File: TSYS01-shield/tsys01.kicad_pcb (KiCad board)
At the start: 2 copper layers, 20 x 24 mm, 25 parts, among them P1 CONN_01X02, P2 CONN_01X04, U1 TSYS01, U2 SP6213

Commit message: First production version
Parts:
- added G***: LOGO, LOGO, F.Cu at (43.1, 57.2)
- added G***: LOGO, LOGO, F.Cu at (43.7, 66.9)
- P1: footprint Pin_Headers:Pin_Header_Angled_1x02 -> pin_header_fork:Pin_Header_Angled_SMD_1x02
- P2: footprint Pin_Headers:Pin_Header_Angled_1x04 -> pin_header_fork:Pin_Header_Angled_SMD_1x04
- moved JP3 9.00 mm to (29.0, 52.1), turned to 270 degrees
- moved JP4 7.97 mm to (29.0, 53.6), turned to 270 degrees
- moved U1 6.94 mm to (34.3, 51.6)
- moved C3 4.50 mm to (30.6, 52.8), turned to 270 degrees
- moved C2 4.04 mm to (31.7, 59.7), turned to 270 degrees
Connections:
- U1 pad 17: (no net) -> /PAD
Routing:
- net +3V3: track 27.7 -> 42.9 mm, vias 4 -> 5
- net GNDA: track 16.4 -> 27.1 mm, vias 8 -> 5
- net Net-(D2-Pad2): track 8.02 -> 16.5 mm
- net Net-(D4-Pad2): track 5.58 -> 13.2 mm
- net Net-(D6-Pad2): track 6.07 -> 13.3 mm
- net /PAD: track 0.00 -> 5.97 mm, vias 0 -> 4
- net /EN: track 9.90 -> 15.4 mm
- net /Vin: track 12.3 -> 11.8 mm, vias 0 -> 2
- added copper zone on B.Cu, net /PAD
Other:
- board size 20 x 24 mm -> 28 x 28 mm
- net class Default: clearance 0.2 -> 0.19
- rule trace_clearance: 0.2 -> 0.19
- board text added: "5V"
- board text added: "CS"
- board text added: "GND"
- board text added: "I2C mode: R2 NO-POP, I2C Address: D8 Pull down OR D9 Pull up"
- board text added: "JMP1: always ON JMP2: ON when CS HIGH !JMP1 & !JMP2: undefined JMP1 & JMP2: short circuit"
- board text added: "JMP3: I2C mode JMP4: SPI mode !JMP3 & !JMP4: undefined JMP3 & JMP4: short circuit"
- board text added: "MISO"
- board text added: "MOSI/SDA"
- board text added: "Open Hardware"
- board text added: "SCLK/SCL"
- board text added: "SPI MODE: JMP1 only"
- board text added: "TSYS01 High precision temperature sensor board"
- board text added: "https://github.com/ ojousima/kon-41.3131"

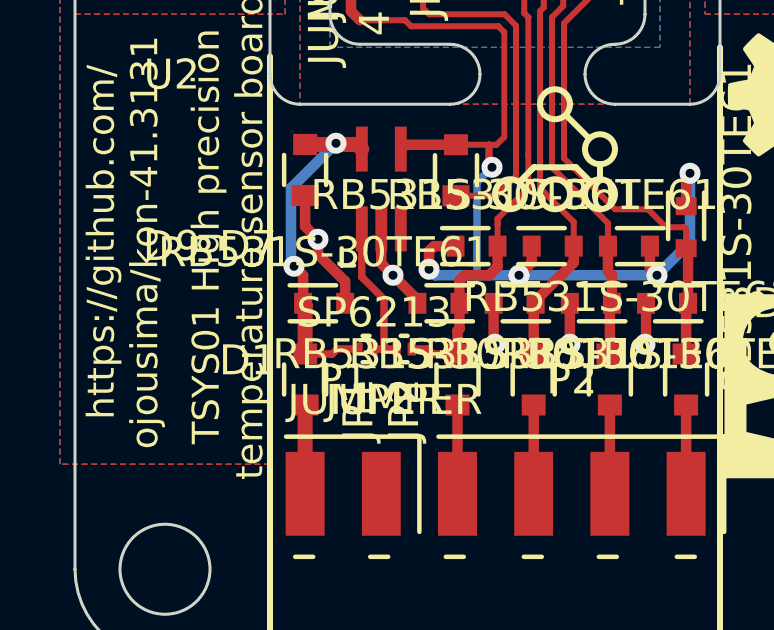
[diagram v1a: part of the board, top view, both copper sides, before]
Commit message: Fix jumper connection
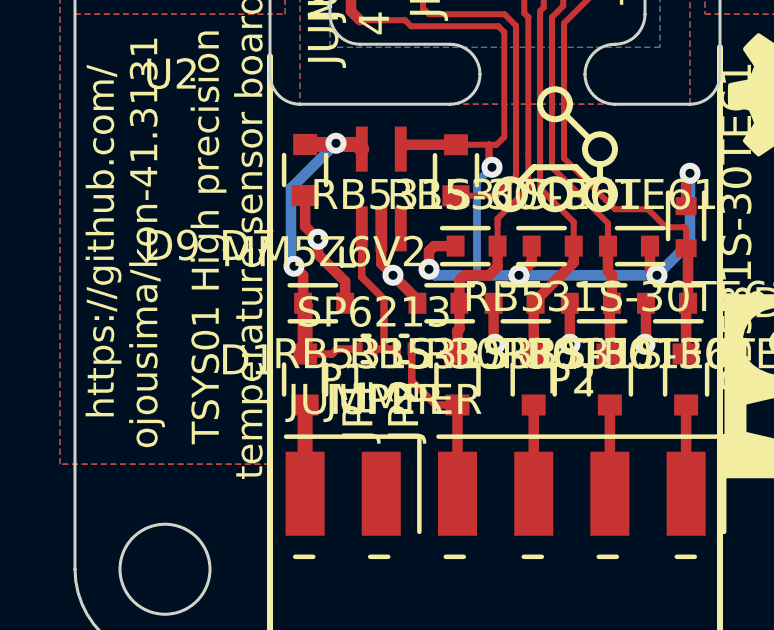
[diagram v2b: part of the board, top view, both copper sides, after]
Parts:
- D1: value RB531S-30TE61 -> MM5Z6V2
- R1, R2, R3, R4, R5: value R -> 220
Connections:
- JP2 pad 2: /EN -> /CS
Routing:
- net /CS: track 2.96 -> 5.88 mm
- net /EN: track 15.4 -> 13.8 mm

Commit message: Fix ground of connector
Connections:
- P1 pad 1: GND -> GNDA

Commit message: Final version
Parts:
- added JP5: JUMPER, Resistors_SMD:R_0201, F.Cu at (36.0, 56.6)
- moved D3 0.10 mm to (39.4, 61.5)
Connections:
- JP1 pad 2: Net-(JP1-Pad2) -> /Vin
- JP2 pad 1: Net-(JP1-Pad2) -> /Vin
- JP3 pad 2: Net-(JP3-Pad2) -> GNDA
- JP4 pad 1: Net-(JP3-Pad2) -> GNDA
- U1 pad 16: Net-(JP3-Pad2) -> GNDA
- U2 pad 1: Net-(JP1-Pad2) -> /Vin
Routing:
- net GNDA: track 27.1 -> 33.6 mm
- net /Vin: track 11.8 -> 17.4 mm
- net Net-(JP1-Pad2): track 5.09 -> 0.00 mm
- net Net-(JP3-Pad2): track 4.38 -> 0.00 mm
- net /PAD: track 5.97 -> 7.58 mm, vias 4 -> 5
- net Net-(D6-Pad2): track 13.3 -> 13.8 mm
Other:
- outline, holes or cut-outs redrawn
